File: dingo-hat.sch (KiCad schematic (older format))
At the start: 56 parts, among them J1 6-18V, J14 NEOPIXEL, J15 MPU-9250, J16 4, J17 5, J18 6, J19 7, J2 Raspberry_Pi_2_3, J24 3mm_Mount, J25 3mm_Mount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

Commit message: Cleaning up libs. Looking at power.
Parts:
- removed G?: LCA2020Logo, symbol graphics:LCA2020Logo
- removed G?: CCHSLogo, symbol graphics:CCHSLogo
- added G?: CCHSLogo, symbol dingo-hat-graphics:CCHSLogo
- added G?: LCA2020Logo, symbol dingo-hat-graphics:LCA2020Logo
- U3: symbol donkey-hat:MPM3632C -> mpm3632:MPM3632C
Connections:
- wire segments 299 -> 298
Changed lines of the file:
@@
 $Descr A4 11693 8268
 encoding utf-8
-Sheet 1 1
+Sheet 1 2
 Title ""
 Date ""
@@
 Connection ~ 4000 850
 $Comp
-L donkey-hat:MPM3632C U3
+L mpm3632:MPM3632C U3
 U 1 1 5C0E66CE
 P 4500 5450
@@
 NoConn ~ 3800 5550
 NoConn ~ 5150 5250
-Wire Wire Line
-	4650 4750 4550 4750
-Connection ~ 4550 4750
-Wire Wire Line
-	4550 4750 4450 4750
 $Comp
 L Device:R R14
@@
 Text Notes 4600 7350 0    118  ~ 24
 Add some I/O protection.
-$Comp
-L graphics:LCA2020Logo G?
-U 1 1 5DA95D6D
-P 600 7200
-F 0 "G?" H 550 7200 50  0000 L CNN
-F 1 "LCA2020Logo" H 600 7200 50  0001 C CNN
-F 2 "" H 600 7200 50  0001 C CNN
-F 3 "" H 600 7200 50  0001 C CNN
-	1    600  7200
-	1    0    0    -1
-$EndComp
-$Comp
-L graphics:CCHSLogo G?
-U 1 1 5DA9B14E
-P 600 7100
-F 0 "G?" H 550 7100 50  0000 L CNN
-F 1 "CCHSLogo" H 600 7100 50  0001 C CNN
-F 2 "" H 600 7100 50  0001 C CNN
-F 3 "" H 600 7100 50  0001 C CNN
-	1    600  7100
-	1    0    0    -1
-$EndComp
 Wire Notes Line
 	1150 7800 1150 6850
@@
 Text Notes 450  6950 0    50   ~ 0
 Graphics/Logos
+$Sheet
+S 1100 4500 950  1050
+U 5DA95EB0
+F0 "Power" 50
+F1 "Power.sch" 50
+$EndSheet
+Wire Wire Line
+	4450 4750 4650 4750
+$Comp
+L dingo-hat-graphics:CCHSLogo G?
+U 1 1 5DB42D44
+P 550 7050
+F 0 "G?" H 628 7050 50  0001 L CNN
+F 1 "CCHSLogo" H 628 7050 50  0000 L CNN
+F 2 "" H 550 7050 50  0001 C CNN
+F 3 "" H 550 7050 50  0001 C CNN
+	1    550  7050
+	1    0    0    -1
+$EndComp
+$Comp
+L dingo-hat-graphics:LCA2020Logo G?
+U 1 1 5DB434D7
+P 550 7200
+F 0 "G?" H 628 7200 50  0001 L CNN
+F 1 "LCA2020Logo" H 628 7200 50  0000 L CNN
+F 2 "" H 550 7200 50  0001 C CNN
+F 3 "" H 550 7200 50  0001 C CNN
+	1    550  7200
+	1    0    0    -1
+$EndComp
 $EndSCHEMATC

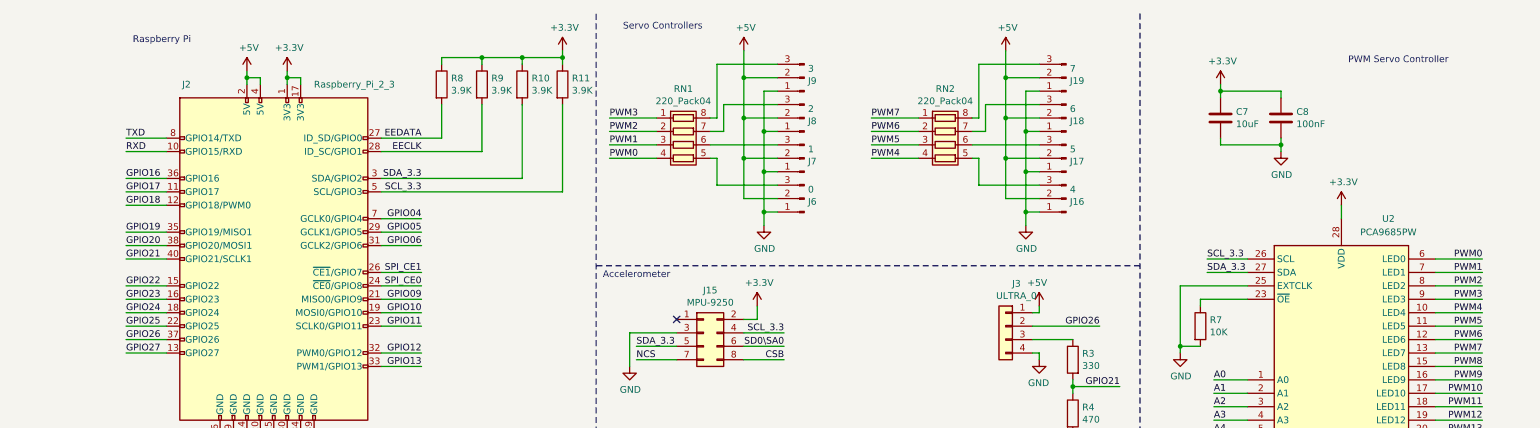
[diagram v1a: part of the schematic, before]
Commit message: Setting up fields, more structure, touching up schematic display properties.
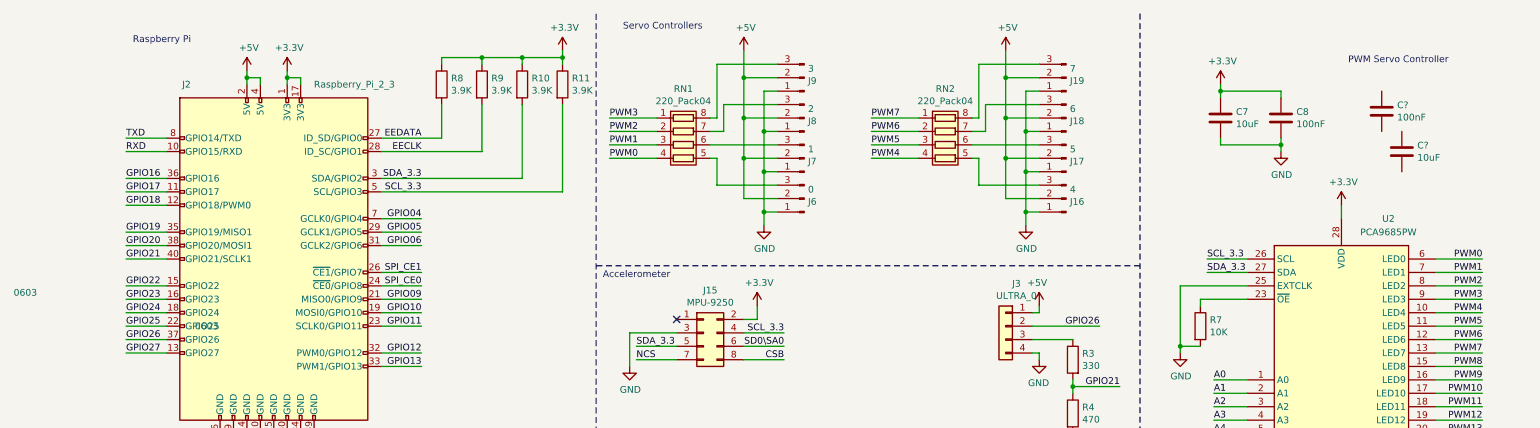
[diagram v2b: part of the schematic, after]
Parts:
- added C?: 100nF, Capacitor_SMD:C_0603_1608Metric_Pad1.05x0.95mm_HandSolder, symbol Device:C
- added C?: 10uF, Capacitor_SMD:C_0603_1608Metric_Pad1.05x0.95mm_HandSolder, symbol Device:C
- C3, C8, C9: Description (none) -> CAP CER 0.1UF 50V X7R 0603; Link (none) -> https://www.digikey.com/product-detail/en/samsung-electro-m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; Supplier 1 (none) -> Digi-Key; Supplier Part Number 1 (none) -> 1276-1000-1-ND; Unit Cost A$ (none) -> 0.15000; Voltage Rating (none) -> 50V
- gave numbers to parts that had none: 2
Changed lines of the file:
@@
 $Descr A4 11693 8268
 encoding utf-8
-Sheet 1 2
+Sheet 1 3
 Title ""
 Date ""
@@
 F 2 "Capacitor_SMD:C_0603_1608Metric_Pad1.05x0.95mm_HandSolder" H 8938 1150 50  0001 C CNN
 F 3 "~" H 8900 1300 50  0001 C CNN
-F 4 "0603" H 0   0   50  0001 C CNN "Package"
+F 4 "0603" H 0   0   50  0000 C CNN "Package"
 	1    8900 1300
 	1    0    0    -1
@@
 F 3 "~" H 4950 7100 50  0001 C CNN
 F 4 "0603" H 1650 -50 50  0001 C CNN "Package"
+F 5 "CAP CER 0.1UF 50V X7R 0603" H 4950 7100 50  0001 C CNN "Description"
+F 6 "50V" H 4950 7100 50  0001 C CNN "Voltage Rating"
+F 7 "https://www.digikey.com/product-detail/en/samsung-electro-mechanics/CL10B104KB8NNNC/1276-1000-1-ND/3889086" H 4950 7100 50  0001 C CNN "Link"
+F 8 "Digi-Key" H 4950 7100 50  0001 C CNN "Supplier 1"
+F 9 "1276-1000-1-ND" H 4950 7100 50  0001 C CNN "Supplier Part Number 1"
+F 10 "0.15000" H 4950 7100 50  0001 C CNN "Unit Cost A$"
 	1    4950 7100
 	1    0    0    -1
@@
 Wire Wire Line
 	4950 6950 4950 6900
-$Comp
-L Device:C C8
-U 1 1 5C185988
-P 9350 1300
-F 0 "C8" H 9465 1346 50  0000 L CNN
-F 1 "100nF" H 9465 1255 50  0000 L CNN
-F 2 "Capacitor_SMD:C_0603_1608Metric_Pad1.05x0.95mm_HandSolder" H 9388 1150 50  0001 C CNN
-F 3 "~" H 9350 1300 50  0001 C CNN
-F 4 "0603" H 0   0   50  0001 C CNN "Package"
-	1    9350 1300
-	1    0    0    -1
-$EndComp
 Wire Wire Line
 	8900 1100 9350 1100
@@
 F 3 "~" H 5250 7100 50  0001 C CNN
 F 4 "0603" H 1650 -50 50  0001 C CNN "Package"
+F 5 "CAP CER 0.1UF 50V X7R 0603" H 5250 7100 50  0001 C CNN "Description"
+F 6 "50V" H 5250 7100 50  0001 C CNN "Voltage Rating"
+F 7 "https://www.digikey.com/product-detail/en/samsung-electro-mechanics/CL10B104KB8NNNC/1276-1000-1-ND/3889086" H 5250 7100 50  0001 C CNN "Link"
+F 8 "Digi-Key" H 5250 7100 50  0001 C CNN "Supplier 1"
+F 9 "1276-1000-1-ND" H 5250 7100 50  0001 C CNN "Supplier Part Number 1"
+F 10 "0.15000" H 5250 7100 50  0001 C CNN "Unit Cost A$"
 	1    5250 7100
 	1    0    0    -1
@@
 	4450 4750 4650 4750
 $Comp
-L dingo-hat-graphics:CCHSLogo G?
+L dingo-hat-graphics:CCHSLogo G1
 U 1 1 5DB42D44
 P 550 7050
-F 0 "G?" H 628 7050 50  0001 L CNN
+F 0 "G1" H 628 7050 50  0001 L CNN
 F 1 "CCHSLogo" H 628 7050 50  0000 L CNN
 F 2 "" H 550 7050 50  0001 C CNN
@@
 $EndComp
 $Comp
-L dingo-hat-graphics:LCA2020Logo G?
+L dingo-hat-graphics:LCA2020Logo G2
 U 1 1 5DB434D7
 P 550 7200
-F 0 "G?" H 628 7200 50  0001 L CNN
+F 0 "G2" H 628 7200 50  0001 L CNN
 F 1 "LCA2020Logo" H 628 7200 50  0000 L CNN
 F 2 "" H 550 7200 50  0001 C CNN
@@
 	1    0    0    -1
 $EndComp
+$Comp
+L Device:C C8
+U 1 1 5C185988
+P 9350 1300
+F 0 "C8" H 9465 1346 50  0000 L CNN
+F 1 "100nF" H 9465 1255 50  0000 L CNN
+F 2 "Capacitor_SMD:C_0603_1608Metric_Pad1.05x0.95mm_HandSolder" H 9388 1150 50  0001 C CNN
+F 3 "~" H 9350 1300 50  0001 C CNN
+F 4 "0603" H 0   0   50  0001 C CNN "Package"
+F 5 "CAP CER 0.1UF 50V X7R 0603" H 9350 1300 50  0001 C CNN "Description"
+F 6 "50V" H 9350 1300 50  0001 C CNN "Voltage Rating"
+F 7 "https://www.digikey.com/product-detail/en/samsung-electro-mechanics/CL10B104KB8NNNC/1276-1000-1-ND/3889086" H 9350 1300 50  0001 C CNN "Link"
+F 8 "Digi-Key" H 9350 1300 50  0001 C CNN "Supplier 1"
+F 9 "1276-1000-1-ND" H 9350 1300 50  0001 C CNN "Supplier Part Number 1"
+F 10 "0.15000" H 9350 1300 50  0001 C CNN "Unit Cost A$"
+	1    9350 1300
+	1    0    0    -1
+$EndComp
+$Comp
+L Device:C C?
+U 1 1 5DB569B9
+P 10100 1250
+F 0 "C?" H 10215 1296 50  0000 L CNN
+F 1 "100nF" H 10215 1205 50  0000 L CNN
+F 2 "Capacitor_SMD:C_0603_1608Metric_Pad1.05x0.95mm_HandSolder" H 10138 1100 50  0001 C CNN
+F 3 "~" H 10100 1250 50  0001 C CNN
+F 4 "0603" H 750 -50 50  0001 C CNN "Package"
+F 5 "CAP CER 0.1UF 50V X7R 0603" H 10100 1250 50  0001 C CNN "Description"
+F 6 "50V" H 10100 1250 50  0001 C CNN "Voltage Rating"
+F 7 "https://www.digikey.com/product-detail/en/samsung-electro-mechanics/CL10B104KB8NNNC/1276-1000-1-ND/3889086" H 10100 1250 50  0001 C CNN "Link"
+F 8 "Digi-Key" H 10100 1250 50  0001 C CNN "Supplier 1"
+F 9 "1276-1000-1-ND" H 10100 1250 50  0001 C CNN "Supplier Part Number 1"
+F 10 "0.15000" H 10100 1250 50  0001 C CNN "Unit Cost A$"
+	1    10100 1250
+	1    0    0    -1
+$EndComp
+$Comp
+L Device:C C?
+U 1 1 5DB8EAA0
+P 10250 1550
+F 0 "C?" H 10365 1596 50  0000 L CNN
+F 1 "10uF" H 10365 1505 50  0000 L CNN
+F 2 "Capacitor_SMD:C_0603_1608Metric_Pad1.05x0.95mm_HandSolder" H 10288 1400 50  0001 C CNN
+F 3 "~" H 10250 1550 50  0001 C CNN
+F 4 "0603" H 1350 250 50  0000 C CNN "Package"
+	1    10250 1550
+	1    0    0    -1
+$EndComp

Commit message: Changing structure, RM old power circuitry.
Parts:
- removed C1: CP, Capacitor_THT:CP_Radial_D5.0mm_P2.50mm, symbol Device:CP
- removed C2: 10uF, Capacitor_SMD:C_1206_3216Metric_Pad1.42x1.75mm_HandSolder, symbol Device:C
- removed C4: 22uF, Capacitor_SMD:C_1206_3216Metric_Pad1.42x1.75mm_HandSolder, symbol Device:C
- removed J5: REG/BYPASS, Connector_PinHeader_2.54mm:PinHeader_1x03_P2.54mm_Vertical, symbol Connector_Generic:Conn_01x03
- removed Q1: IRLML6401, Package_TO_SOT_SMD:SOT-23_Handsoldering, symbol Transistor_FET:IRLML6402
- removed R12: 1K, Resistor_SMD:R_0603_1608Metric_Pad1.05x0.95mm_HandSolder, symbol Device:R
- removed R13: 47K, Resistor_SMD:R_0603_1608Metric_Pad1.05x0.95mm_HandSolder, symbol Device:R
- removed R14: 8.87K, Resistor_SMD:R_0603_1608Metric_Pad1.05x0.95mm_HandSolder, symbol Device:R
- removed R15: 100K, Resistor_SMD:R_0603_1608Metric_Pad1.05x0.95mm_HandSolder, symbol Device:R
- removed U3: MPM3632C, libs:mpm3632c, symbol mpm3632:MPM3632C
- added Q?: IRLML6401, Package_TO_SOT_SMD:SOT-23_Handsoldering, symbol Transistor_FET:IRLML6402
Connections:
- net labels removed: REG, VIN, VIN_REG
- wire segments 298 -> 245
- no-connect marks 10 -> 7
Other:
- note removed: "6-20V 3A switch mode regulator\n"
- moved on the sheet: J1

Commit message: Battery work, need to get on to connectors.
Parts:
- added J5: LiPo/NiMH, Connector_PinHeader_2.54mm:PinHeader_1x03_P2.54mm_Vertical, symbol Connector_Generic:Conn_01x03
- gave numbers to parts that had none: 3
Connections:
- new net BatterySupply: J5.2 (Pin_2)
- new net LiPoPwr: J5.1 (Pin_1)
- new net NiMHPwr: J5.3 (Pin_3)
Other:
- moved on the sheet: Q401
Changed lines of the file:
@@
 Text Notes 450  6950 0    50   ~ 0
 Graphics/Logos
-$Sheet
-S 4600 4500 950  1050
-U 5DA95EB0
-F0 "Power" 50
-F1 "Power.sch" 50
-$EndSheet
 $Comp
 L dingo-hat-graphics:CCHSLogo G1
@@
 $EndComp
 $Comp
-L Device:C C?
+L Device:C C402
 U 1 1 5DB569B9
 P 10100 1250
-F 0 "C?" H 10215 1296 50  0000 L CNN
+F 0 "C402" H 10215 1296 50  0000 L CNN
 F 1 "100nF" H 10215 1205 50  0000 L CNN
 F 2 "Capacitor_SMD:C_0603_1608Metric_Pad1.05x0.95mm_HandSolder" H 10138 1100 50  0001 C CNN
@@
 $EndComp
 $Comp
-L Device:C C?
+L Device:C C403
 U 1 1 5DB8EAA0
 P 10250 1550
-F 0 "C?" H 10365 1596 50  0000 L CNN
+F 0 "C403" H 10365 1596 50  0000 L CNN
 F 1 "10uF" H 10365 1505 50  0000 L CNN
 F 2 "Capacitor_SMD:C_0603_1608Metric_Pad1.05x0.95mm_HandSolder" H 10288 1400 50  0001 C CNN
@@
 $EndComp
 $Comp
-L Transistor_FET:IRLML6402 Q?
+L Transistor_FET:IRLML6402 Q401
 U 1 1 5DC2606F
-P 6200 4300
-F 0 "Q?" V 6543 4300 50  0000 C CNN
-F 1 "IRLML6401" V 6452 4300 50  0000 C CNN
-F 2 "Package_TO_SOT_SMD:SOT-23_Handsoldering" H 6400 4225 50  0001 L CIN
-F 3 "https://www.infineon.com/dgdl/irlml6402pbf.pdf?fileId=5546d462533600a401535668d5c2263c" H 6200 4300 50  0001 L CNN
-F 4 "https://www.digikey.com.au/product-detail/en/infineon-technologies/IRLML6401TRPBF/IRLML6401PBFCT-ND/812509" V 6200 4300 50  0001 C CNN "Link"
-F 5 "SOT-23" H -450 -1150 50  0001 C CNN "Package"
-F 6 "International Rectifier" H -450 -1150 50  0001 C CNN "Manufacturer"
-F 7 "IRLML6402PbF" H -450 -1150 50  0001 C CNN "Mfg Part #"
-	1    6200 4300
+P -400 4050
+F 0 "Q401" V -57 4050 50  0000 C CNN
+F 1 "IRLML6401" V -148 4050 50  0000 C CNN
+F 2 "Package_TO_SOT_SMD:SOT-23_Handsoldering" H -200 3975 50  0001 L CIN
+F 3 "https://www.infineon.com/dgdl/irlml6402pbf.pdf?fileId=5546d462533600a401535668d5c2263c" H -400 4050 50  0001 L CNN
+F 4 "https://www.digikey.com.au/product-detail/en/infineon-technologies/IRLML6401TRPBF/IRLML6401PBFCT-ND/812509" V -400 4050 50  0001 C CNN "Link"
+F 5 "SOT-23" H -7050 -1400 50  0001 C CNN "Package"
+F 6 "International Rectifier" H -7050 -1400 50  0001 C CNN "Manufacturer"
+F 7 "IRLML6402PbF" H -7050 -1400 50  0001 C CNN "Mfg Part #"
+	1    -400 4050
 	0    -1   -1   0
 $EndComp
 $Sheet
-S 3400 4450 950  1100
+S 5950 5100 950  1050
+U 5DA95EB0
+F0 "Power" 50
+F1 "Power.sch" 50
+$EndSheet
+Wire Notes Line
+	7300 6500 7300 4900
+Text Label 3900 5300 2    50   ~ 0
+NiMHPwr
+Text Label 3900 5500 2    50   ~ 0
+LiPoPwr
+$Comp
+L Connector_Generic:Conn_01x03 J5
+U 1 1 5C1E72E1
+P 3350 5400
+F 0 "J5" H 3270 5075 50  0000 C CNN
+F 1 "LiPo/NiMH" H 3270 5166 50  0000 C CNN
+F 2 "Connector_PinHeader_2.54mm:PinHeader_1x03_P2.54mm_Vertical" H 3350 5400 50  0001 C CNN
+F 3 "~" H 3350 5400 50  0001 C CNN
+	1    3350 5400
+	-1   0    0    1
+$EndComp
+Text Label 4100 5400 2    50   ~ 0
+BatterySupply
+$Sheet
+S 1750 4500 950  1100
 U 5DC297AB
-F0 "Battery" 50
+F0 "LiPoBatteryMgmt" 50
 F1 "BatteryManagement.sch" 50
+F2 "Batt+" U L 1750 4750 50
+F3 "Pack-" U R 2700 5200 50
+F4 "Batt-" U L 1750 5200 50
 $EndSheet
+Wire Wire Line
+	3550 5300 3900 5300
+Wire Wire Line
+	3550 5500 3900 5500
+Wire Wire Line
+	3550 5400 4100 5400
+$Comp
+L power:GND #PWR0401
+U 1 1 5DE52CD2
+P 2950 5350
+F 0 "#PWR0401" H 2950 5100 50  0001 C CNN
+F 1 "GND" H 2955 5177 50  0000 C CNN
+F 2 "" H 2950 5350 50  0001 C CNN
+F 3 "" H 2950 5350 50  0001 C CNN
+	1    2950 5350
+	1    0    0    -1
+$EndComp
+Wire Wire Line
+	2950 5350 2950 5200
+Wire Wire Line
+	2700 5200 2950 5200
 $EndSCHEMATC

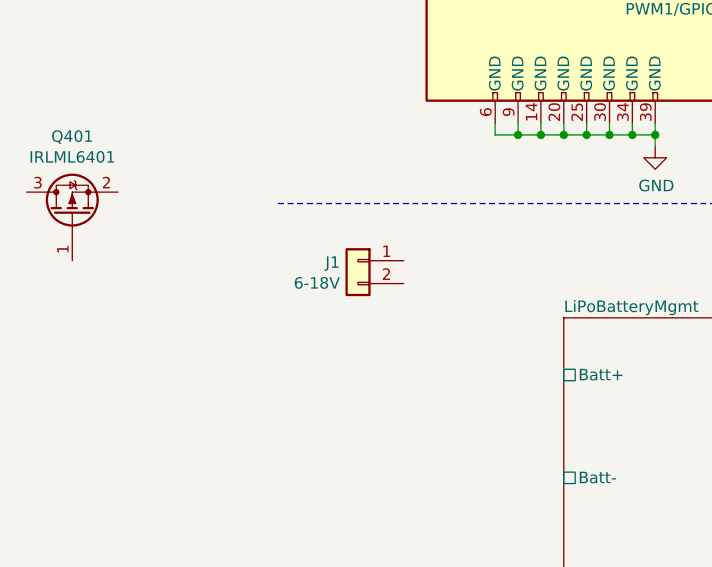
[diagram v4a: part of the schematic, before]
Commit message: Charging. Do balance next if including.
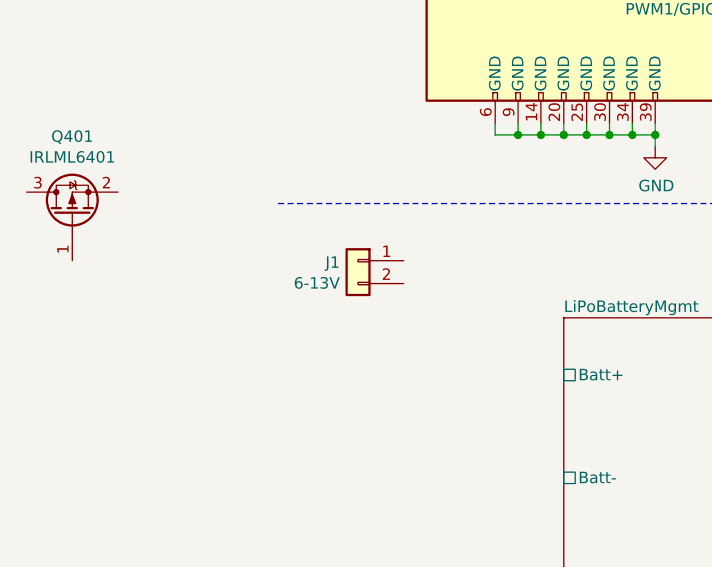
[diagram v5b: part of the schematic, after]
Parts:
- J1: value 6-18V -> 6-13V
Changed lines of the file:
@@
 P 850 4250
 F 0 "J1" H 929 4242 50  0000 L CNN
-F 1 "6-18V" H 929 4151 50  0000 L CNN
+F 1 "6-13V" H 929 4151 50  0000 L CNN
 F 2 "Connector_Phoenix_MC:PhoenixContact_MC_1,5_2-G-3.5_1x02_P3.50mm_Horizontal" H 850 4250 50  0001 C CNN
 F 3 "~" H 850 4250 50  0001 C CNN
